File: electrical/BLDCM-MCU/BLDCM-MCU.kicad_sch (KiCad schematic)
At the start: 85 parts, among them J1 52991-0308, K1 EVPAKE31A, U1 STM32F446RE, U10 SK6805, U11 SK6805, U12 SK6805, U13 SK6805, U14 SK6805, U15 SK6805, U16 SK6805, U17 SK6805, U18 SK6805, U19 SK6805, U2 SN74LV1T34DBVR, U20 MT6701, U3 ISM330DHCX, U4 SK6805, U5 SK6805, U6 SK6805, U7 SK6805, U8 SK6805, U9 SK6805, Y1 ECS-3225MVLC-240-CN

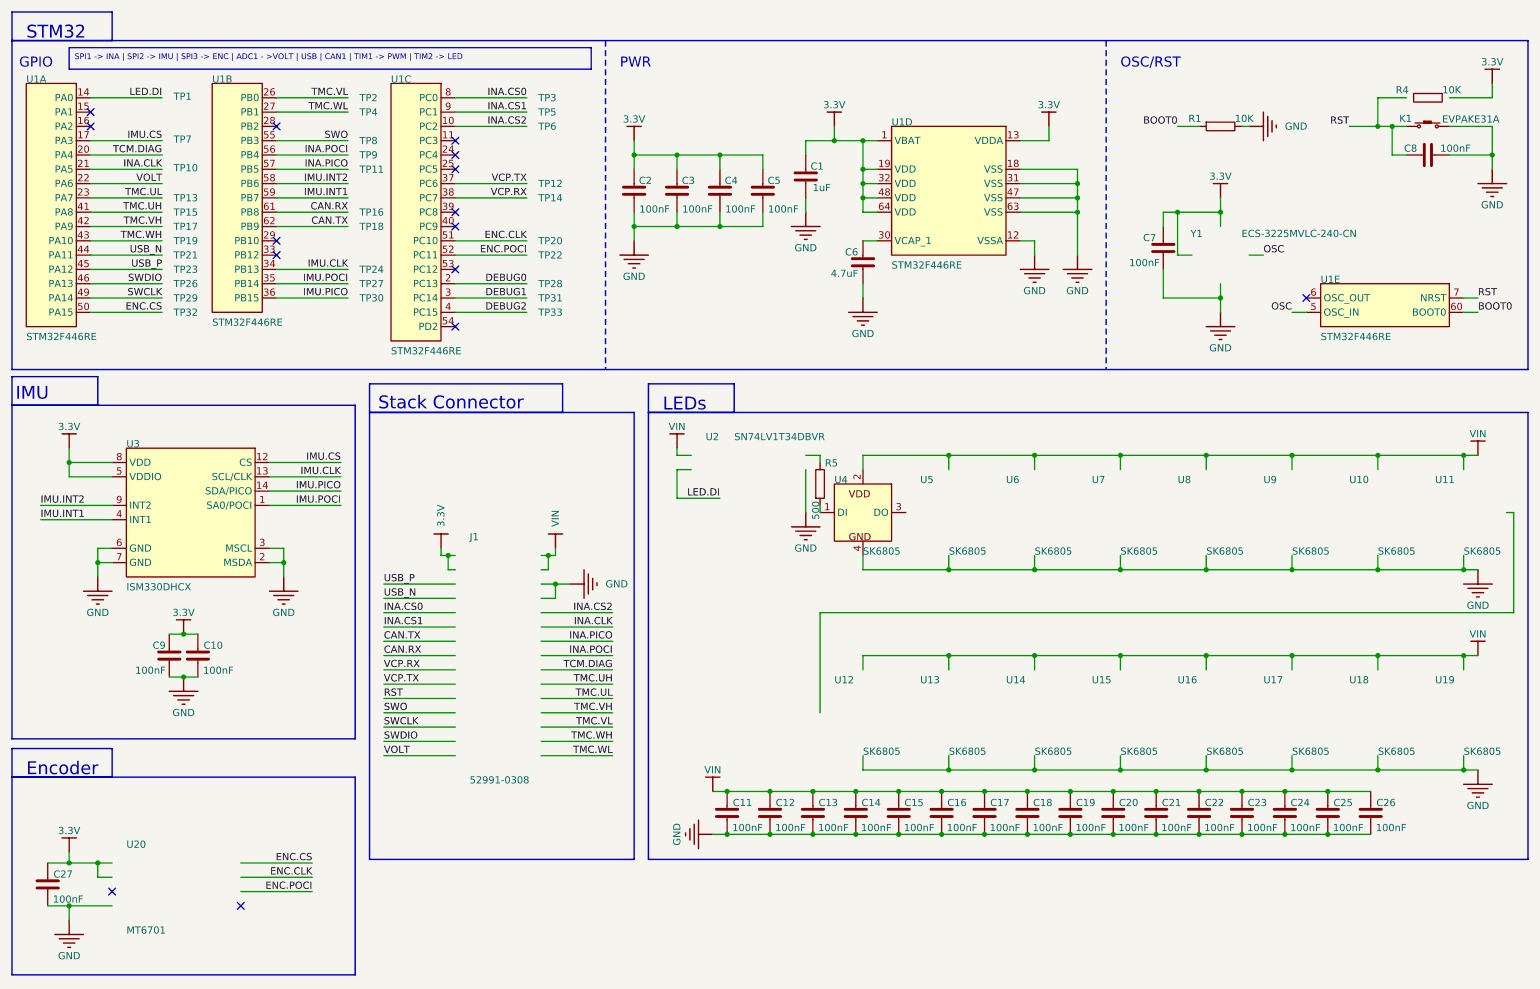
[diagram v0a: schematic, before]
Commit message: Fix: BLDCM-MCU ERC errors
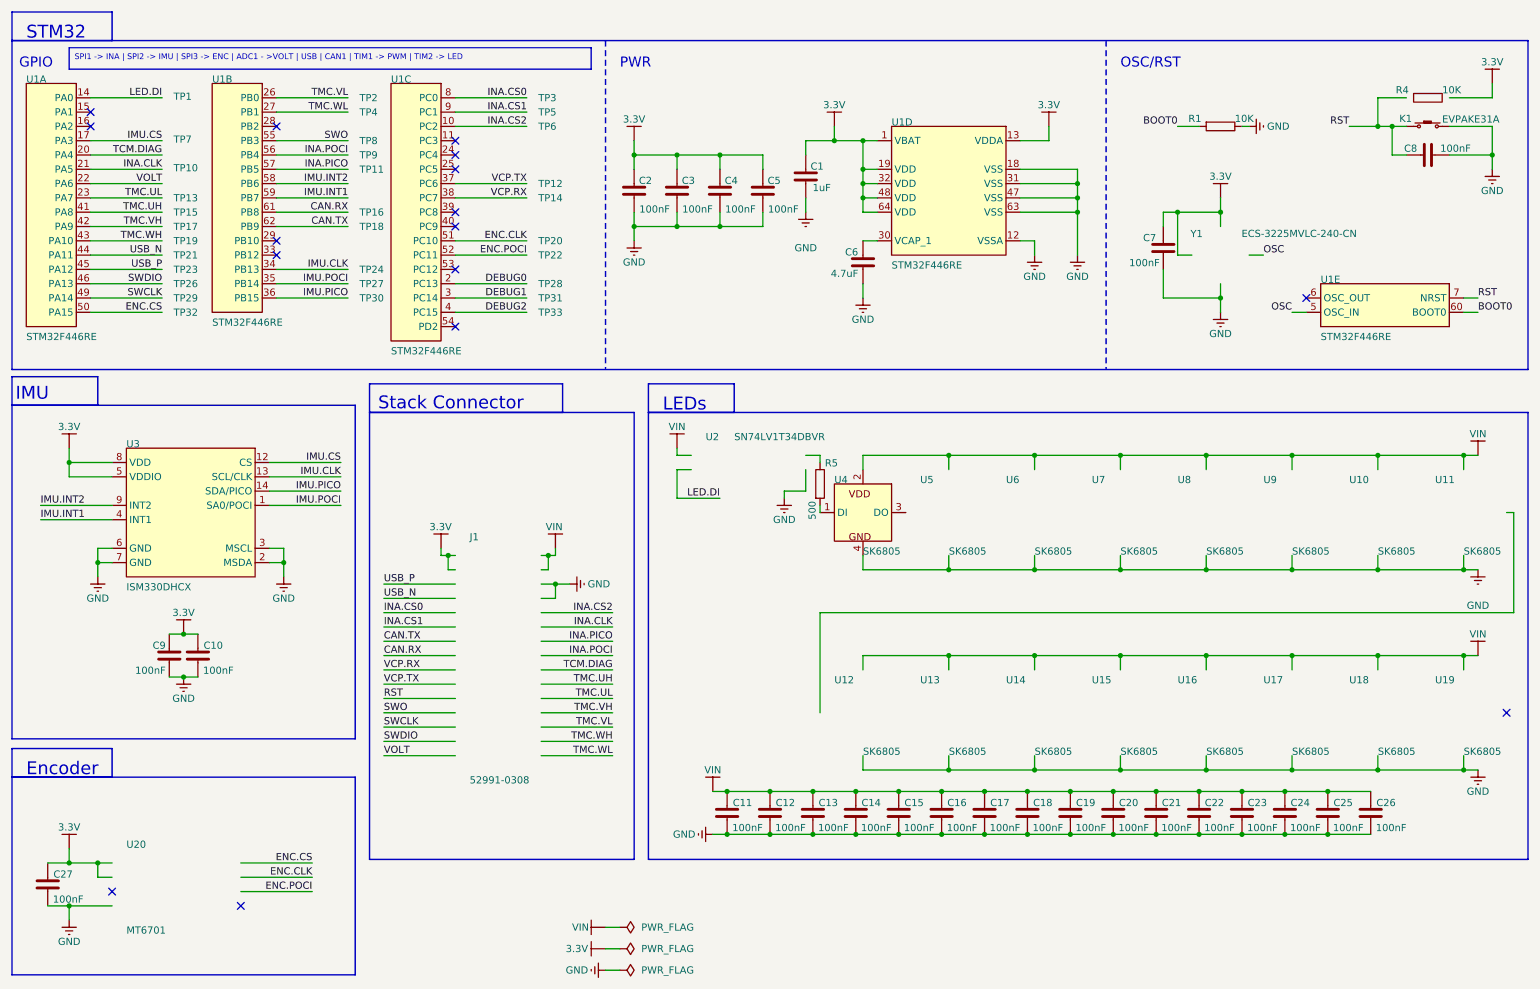
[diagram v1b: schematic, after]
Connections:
- no-connect marks 15 -> 16
